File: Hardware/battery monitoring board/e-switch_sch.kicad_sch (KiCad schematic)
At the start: 5 parts, among them K1 Relay_SPST-NO, Q2 PN2222A

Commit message: added programmable LED and reference updates
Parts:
- renumbered D4 to D5, R14 to R15, R15 to R16
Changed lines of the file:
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@@
   (symbol (lib_id "power:GND") (at 86.36 88.9 0) (unit 1)
     (in_bom yes) (on_board yes) (dnp no) (fields_autoplaced)
-    (property "Reference" "#PWR023" (at 86.36 95.25 0)
+    (property "Reference" "#PWR024" (at 86.36 95.25 0)
       (effects (font (size 1.27 1.27)) hide)
     )
@@
       (project "battery monitoring board"
         (path "/bf623d80-ca5a-491f-9daa-4dffbeba5279/d1e89632-1041-42ed-815d-03472eda859a"
-          (reference "#PWR023") (unit 1)
+          (reference "#PWR024") (unit 1)
         )
       )
@@
   (symbol (lib_id "Device:R_US") (at 62.23 71.12 90) (unit 1)
     (in_bom yes) (on_board yes) (dnp no) (fields_autoplaced)
-    (property "Reference" "R14" (at 62.23 64.77 90)
+    (property "Reference" "R15" (at 62.23 64.77 90)
       (effects (font (size 1.27 1.27)))
     )
@@
       (project "battery monitoring board"
         (path "/bf623d80-ca5a-491f-9daa-4dffbeba5279/d1e89632-1041-42ed-815d-03472eda859a"
-          (reference "R14") (unit 1)
+          (reference "R15") (unit 1)
         )
       )
@@
   (symbol (lib_id "Device:D") (at 72.39 58.42 0) (unit 1)
     (in_bom yes) (on_board yes) (dnp no)
-    (property "Reference" "D4" (at 72.39 53.848 0)
+    (property "Reference" "D5" (at 72.39 53.848 0)
       (effects (font (size 1.27 1.27)))
     )
@@
       (project "battery monitoring board"
         (path "/bf623d80-ca5a-491f-9daa-4dffbeba5279/d1e89632-1041-42ed-815d-03472eda859a"
-          (reference "D4") (unit 1)
+          (reference "D5") (unit 1)
         )
       )
@@
   (symbol (lib_id "Device:R_US") (at 71.12 80.01 0) (unit 1)
     (in_bom yes) (on_board yes) (dnp no) (fields_autoplaced)
-    (property "Reference" "R15" (at 73.66 78.74 0)
+    (property "Reference" "R16" (at 73.66 78.74 0)
       (effects (font (size 1.27 1.27)) (justify left))
     )
@@
       (project "battery monitoring board"
         (path "/bf623d80-ca5a-491f-9daa-4dffbeba5279/d1e89632-1041-42ed-815d-03472eda859a"
-          (reference "R15") (unit 1)
+          (reference "R16") (unit 1)
         )
       )
@@
   (symbol (lib_id "PCM_4ms_Power-symbol:+9V") (at 49.53 45.72 90) (unit 1)
     (in_bom yes) (on_board yes) (dnp no) (fields_autoplaced)
-    (property "Reference" "#PWR022" (at 53.34 45.72 0)
+    (property "Reference" "#PWR023" (at 53.34 45.72 0)
       (effects (font (size 1.27 1.27)) hide)
     )
@@
       (project "battery monitoring board"
         (path "/bf623d80-ca5a-491f-9daa-4dffbeba5279/d1e89632-1041-42ed-815d-03472eda859a"
-          (reference "#PWR022") (unit 1)
+          (reference "#PWR023") (unit 1)
         )
       )

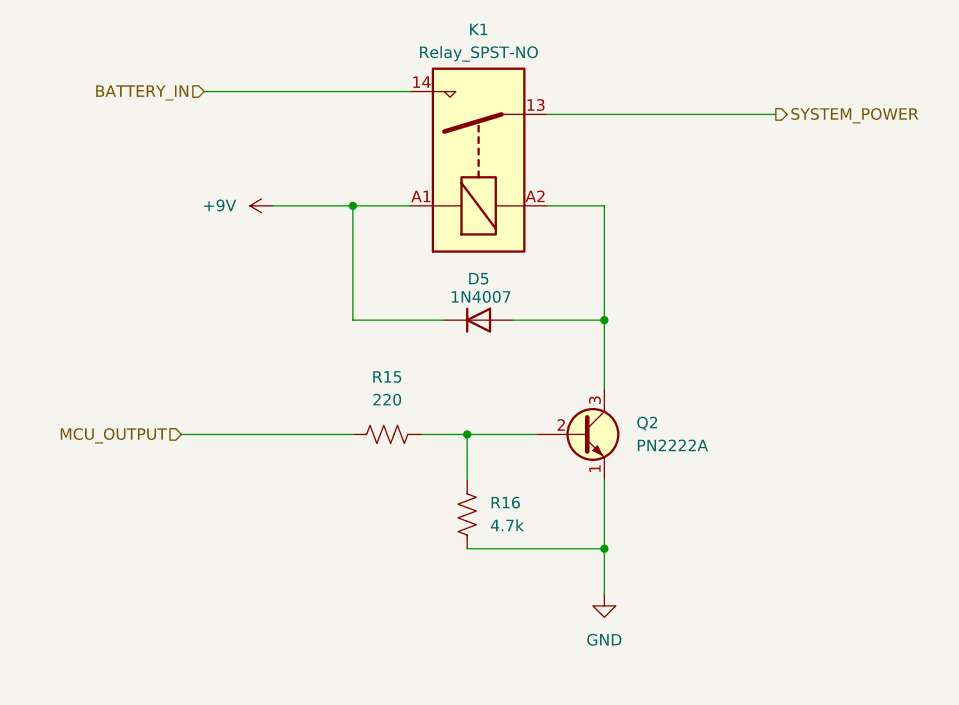
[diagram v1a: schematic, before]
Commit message: added test points (battery monitoring)
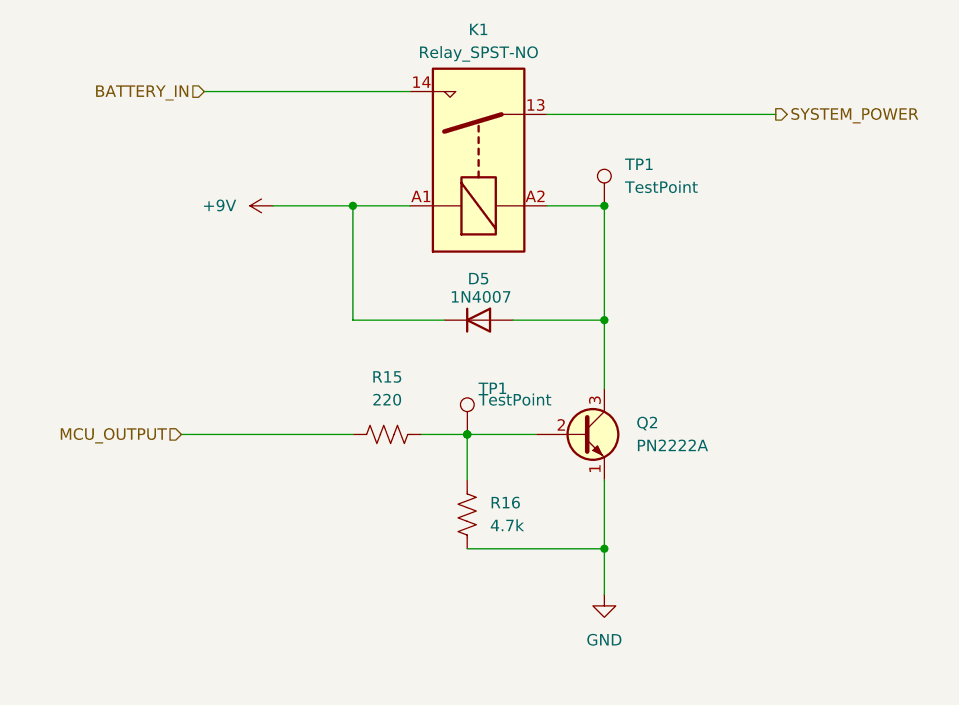
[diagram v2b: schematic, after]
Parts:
- added TP1 (x2): TestPoint, symbol Connector:TestPoint
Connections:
- net at Q2.2 (B), R15.2, R16.1: now also TP1.1
- net at D5.2 (A), K1.A2, Q2.3 (C): now also TP1.1
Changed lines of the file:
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@@
 (kicad_sch (version 20230121) (generator eeschema)
   (paper "A4")
+  (junction (at 86.36 45.72) (diameter 0) (color 0 0 0 0)
+  )
+  (junction (at 71.1341 71.12) (diameter 0) (color 0 0 0 0)
+  )
   (junction (at 86.36 58.42) (diameter 0) (color 0 0 0 0)
   )
@@
     (stroke (width 0) (type default))
   )
-  (wire (pts (xy 71.12 71.12) (xy 78.74 71.12))
+  (wire (pts (xy 71.12 71.12) (xy 71.1341 71.12))
     (stroke (width 0) (type default))
   )
@@
   )
   (wire (pts (xy 39.37 71.12) (xy 58.42 71.12))
+    (stroke (width 0) (type default))
+  )
+  (wire (pts (xy 71.1341 71.12) (xy 78.74 71.12))
     (stroke (width 0) (type default))
   )
@@
   (hierarchical_label "SYSTEM_POWER" (shape output) (at 105.41 35.56 0) (fields_autoplaced)
     (effects (font (size 1.27 1.27)) (justify left))
+  )
+  (symbol (lib_id "Connector:TestPoint") (at 86.36 45.72 0) (unit 1)
+    (in_bom yes) (on_board yes) (dnp no) (fields_autoplaced)
+    (property "Reference" "TP1" (at 88.6629 41.148 0)
+      (effects (font (size 1.27 1.27)) (justify left))
+    )
+    (property "Value" "TestPoint" (at 88.6629 43.688 0)
+      (effects (font (size 1.27 1.27)) (justify left))
+    )
+    (property "Footprint" "" (at 91.44 45.72 0)
+      (effects (font (size 1.27 1.27)) hide)
+    )
+    (property "Datasheet" "~" (at 91.44 45.72 0)
+      (effects (font (size 1.27 1.27)) hide)
+    )
+    (pin "1")
+    (instances
+      (project "battery monitoring board"
+        (path "/bf623d80-ca5a-491f-9daa-4dffbeba5279/5ec2dbdf-a276-4d4c-99fc-008475c1e770"
+          (reference "TP1") (unit 1)
+        )
+        (path "/bf623d80-ca5a-491f-9daa-4dffbeba5279/d1e89632-1041-42ed-815d-03472eda859a"
+          (reference "TP13") (unit 1)
+        )
+      )
+    )
   )
   (symbol (lib_id "power:GND") (at 86.36 88.9 0) (unit 1)
@@
         )
       )
+    )
+  )
+  (symbol (lib_id "Connector:TestPoint") (at 71.1341 71.12 0) (unit 1)
+    (in_bom yes) (on_board yes) (dnp no)
+    (property "Reference" "TP1" (at 72.39 66.04 0)
+      (effects (font (size 1.27 1.27)) (justify left))
+    )
+    (property "Value" "TestPoint" (at 72.39 67.31 0)
+      (effects (font (size 1.27 1.27)) (justify left))
+    )
+    (property "Footprint" "" (at 76.2141 71.12 0)
+      (effects (font (size 1.27 1.27)) hide)
+    )
+    (property "Datasheet" "~" (at 76.2141 71.12 0)
+      (effects (font (size 1.27 1.27)) hide)
+    )
+    (pin "1")
+    (instances
+      (project "battery monitoring board"
+        (path "/bf623d80-ca5a-491f-9daa-4dffbeba5279/5ec2dbdf-a276-4d4c-99fc-008475c1e770"
+          (reference "TP1") (unit 1)
+        )
+        (path "/bf623d80-ca5a-491f-9daa-4dffbeba5279/d1e89632-1041-42ed-815d-03472eda859a"
+          (reference "TP12") (unit 1)
+        )
+      )

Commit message: Added footprints to battery monitoring
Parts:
- D5: footprint (none) -> Diode_SMD:D_0805_2012Metric_Pad1.15x1.40mm_HandSolder
- K1: footprint (none) -> Library:Relay
- R15, R16: footprint (none) -> Resistor_SMD:R_0805_2012Metric_Pad1.20x1.40mm_HandSolder
- TP1: footprint (none) -> Library:Test Pads
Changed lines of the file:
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@@
       (effects (font (size 1.27 1.27)) (justify left))
     )
-    (property "Footprint" "" (at 91.44 45.72 0)
+    (property "Footprint" "Library:Test Pads" (at 91.44 45.72 0)
       (effects (font (size 1.27 1.27)) hide)
     )
@@
       (effects (font (size 1.27 1.27)) (justify left))
     )
-    (property "Footprint" "" (at 76.2141 71.12 0)
+    (property "Footprint" "Library:Test Pads" (at 76.2141 71.12 0)
       (effects (font (size 1.27 1.27)) hide)
     )
@@
       (effects (font (size 1.27 1.27)))
     )
-    (property "Footprint" "" (at 62.484 70.104 90)
+    (property "Footprint" "Resistor_SMD:R_0805_2012Metric_Pad1.20x1.40mm_HandSolder" (at 62.484 70.104 90)
       (effects (font (size 1.27 1.27)) hide)
     )
@@
       (effects (font (size 1.27 1.27)))
     )
-    (property "Footprint" "" (at 72.39 58.42 0)
+    (property "Footprint" "Diode_SMD:D_0805_2012Metric_Pad1.15x1.40mm_HandSolder" (at 72.39 58.42 0)
       (effects (font (size 1.27 1.27)) hide)
     )
@@
       (effects (font (size 1.27 1.27)))
     )
-    (property "Footprint" "" (at 73.66 29.21 0)
+    (property "Footprint" "Library:Relay" (at 73.66 29.21 0)
       (effects (font (size 1.27 1.27)) (justify left) hide)
     )
@@
       (effects (font (size 1.27 1.27)) (justify left))
     )
-    (property "Footprint" "" (at 72.136 80.264 90)
+    (property "Footprint" "Resistor_SMD:R_0805_2012Metric_Pad1.20x1.40mm_HandSolder" (at 72.136 80.264 90)
       (effects (font (size 1.27 1.27)) hide)
     )

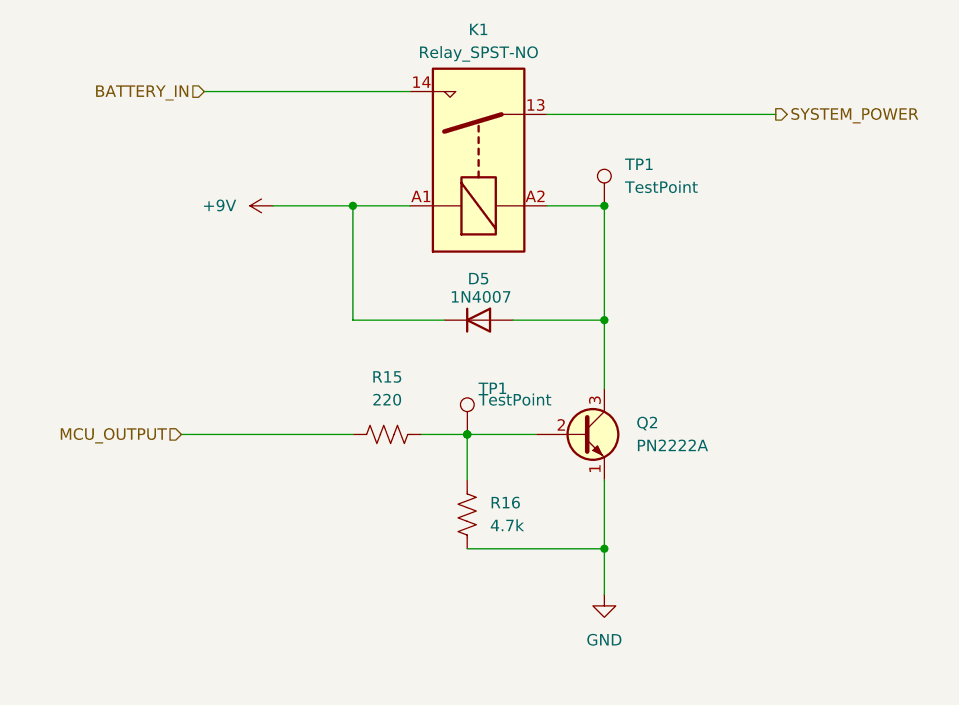
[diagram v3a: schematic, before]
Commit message: Added screw holes + other stuff
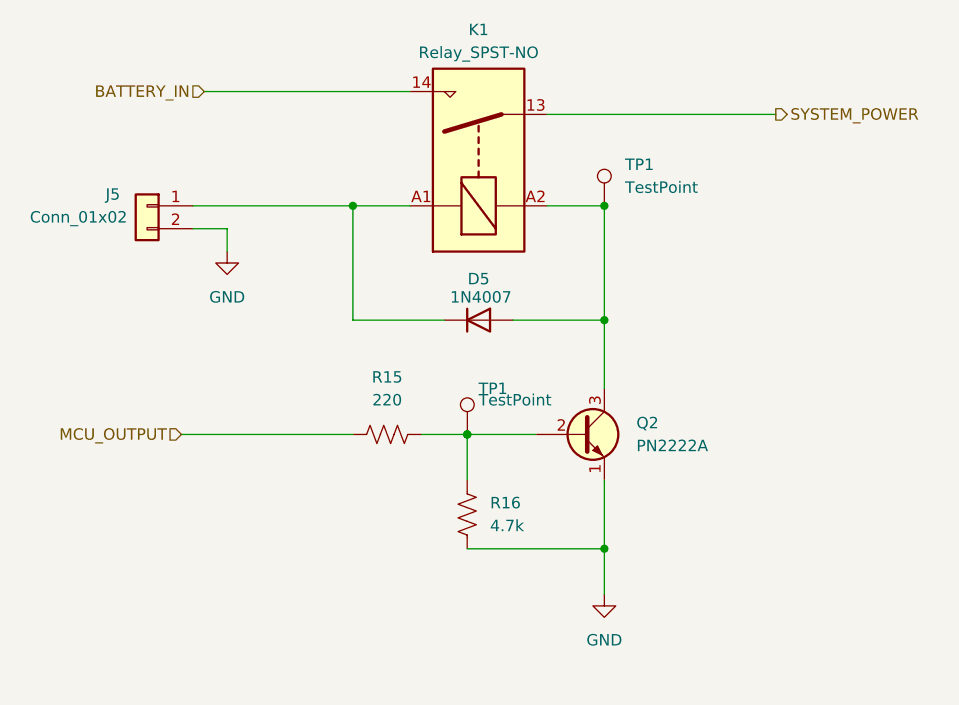
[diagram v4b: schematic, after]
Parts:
- added J5: Conn_01x02, Library:JST_BM02B-GHS-TBT_LF__SN_, symbol Connector_Generic:Conn_01x02
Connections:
- net GND: now also J5.2 (Pin_2)
- net +9V: no longer names the net of D5.1 (K), K1.A1
- net +9V: now also J5.1 (Pin_1)
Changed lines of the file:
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@@
     (stroke (width 0) (type default))
   )
-  (wire (pts (xy 49.53 45.72) (xy 58.42 45.72))
+  (wire (pts (xy 40.64 45.72) (xy 58.42 45.72))
     (stroke (width 0) (type default))
   )
@@
     (stroke (width 0) (type default))
   )
+  (wire (pts (xy 44.45 48.26) (xy 44.45 50.8))
+    (stroke (width 0) (type default))
+  )
   (wire (pts (xy 76.2 58.42) (xy 86.36 58.42))
     (stroke (width 0) (type default))
@@
   )
   (wire (pts (xy 58.42 45.72) (xy 64.77 45.72))
+    (stroke (width 0) (type default))
+  )
+  (wire (pts (xy 40.64 48.26) (xy 44.45 48.26))
     (stroke (width 0) (type default))
   )
@@
         (path "/bf623d80-ca5a-491f-9daa-4dffbeba5279/d1e89632-1041-42ed-815d-03472eda859a"
           (reference "Q2") (unit 1)
+        )
+      )
+    )
+  )
+  (symbol (lib_id "Connector_Generic:Conn_01x02") (at 35.56 45.72 0) (mirror y) (unit 1)
+    (in_bom yes) (on_board yes) (dnp no)
+    (property "Reference" "J5" (at 31.75 44.45 0)
+      (effects (font (size 1.27 1.27)))
+    )
+    (property "Value" "Conn_01x02" (at 27.94 46.99 0)
+      (effects (font (size 1.27 1.27)))
+    )
+    (property "Footprint" "Library:JST_BM02B-GHS-TBT_LF__SN_" (at 35.56 45.72 0)
+      (effects (font (size 1.27 1.27)) hide)
+    )
+    (property "Datasheet" "~" (at 35.56 45.72 0)
+      (effects (font (size 1.27 1.27)) hide)
+    )
+    (pin "1")
+    (pin "2")
+    (instances
+      (project "leak sensor"
+        (path "/127822e7-fd70-4fb4-952a-2fa8fdde2438"
+          (reference "J5") (unit 1)
+        )
+      )
+      (project "battery monitoring board"
+        (path "/bf623d80-ca5a-491f-9daa-4dffbeba5279/7fa71be0-4e2c-431c-85f4-b0f15423b53d"
+          (reference "J8") (unit 1)
+        )
+        (path "/bf623d80-ca5a-491f-9daa-4dffbeba5279/d1e89632-1041-42ed-815d-03472eda859a"
+          (reference "J10") (unit 1)
+        )
+      )
+    )
+  )
+  (symbol (lib_id "PCM_4ms_Power-symbol:GND") (at 44.45 50.8 0) (unit 1)
+    (in_bom yes) (on_board yes) (dnp no) (fields_autoplaced)
+    (property "Reference" "#PWR023" (at 44.45 57.15 0)
+      (effects (font (size 1.27 1.27)) hide)
+    )
+    (property "Value" "GND" (at 44.45 55.88 0)
+      (effects (font (size 1.27 1.27)))
+    )
+    (property "Footprint" "" (at 44.45 50.8 0)
+      (effects (font (size 1.27 1.27)) hide)
+    )
+    (property "Datasheet" "" (at 44.45 50.8 0)
+      (effects (font (size 1.27 1.27)) hide)
+    )
+    (pin "1")
+    (instances
+      (project "battery monitoring board"
+        (path "/bf623d80-ca5a-491f-9daa-4dffbeba5279/d1e89632-1041-42ed-815d-03472eda859a"
+          (reference "#PWR023") (unit 1)
         )
       )
@@
         )
       )
-    )
-  )
-  (symbol (lib_id "PCM_4ms_Power-symbol:+9V") (at 49.53 45.72 90) (unit 1)
-    (in_bom yes) (on_board yes) (dnp no) (fields_autoplaced)
-    (property "Reference" "#PWR023" (at 53.34 45.72 0)
-      (effects (font (size 1.27 1.27)) hide)
-    )
-    (property "Value" "+9V" (at 45.466 45.72 90)
-      (effects (font (size 1.27 1.27)) (justify left))
-    )
-    (property "Footprint" "" (at 49.53 45.72 0)
-      (effects (font (size 1.27 1.27)) hide)
-    )
-    (property "Datasheet" "" (at 49.53 45.72 0)
-      (effects (font (size 1.27 1.27)) hide)
-    )
-    (pin "1")
-    (instances
-      (project "battery monitoring board"
-        (path "/bf623d80-ca5a-491f-9daa-4dffbeba5279/d1e89632-1041-42ed-815d-03472eda859a"
-          (reference "#PWR023") (unit 1)
-        )
-      )

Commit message: silkscreen
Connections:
- net +9V: now reaches D5.1 (K), J5.1 (Pin_1), K1.A1
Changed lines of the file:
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@@
   (junction (at 86.36 83.82) (diameter 0) (color 0 0 0 0)
   )
+  (junction (at 44.45 45.72) (diameter 0) (color 0 0 0 0)
+  )
   (wire (pts (xy 86.36 76.2) (xy 86.36 83.82))
     (stroke (width 0) (type default))
@@
     (stroke (width 0) (type default))
   )
-  (wire (pts (xy 40.64 45.72) (xy 58.42 45.72))
+  (wire (pts (xy 40.64 45.72) (xy 44.45 45.72))
     (stroke (width 0) (type default))
   )
@@
     (stroke (width 0) (type default))
   )
+  (wire (pts (xy 44.45 45.72) (xy 58.42 45.72))
+    (stroke (width 0) (type default))
+  )
   (wire (pts (xy 86.36 83.82) (xy 86.36 88.9))
     (stroke (width 0) (type default))
@@
   )
   (wire (pts (xy 71.1341 71.12) (xy 78.74 71.12))
+    (stroke (width 0) (type default))
+  )
+  (wire (pts (xy 44.45 44.45) (xy 44.45 45.72))
     (stroke (width 0) (type default))
   )
@@
         )
       )
+    )
+  )
+  (symbol (lib_id "PCM_4ms_Power-symbol:+9V") (at 44.45 44.45 0) (unit 1)
+    (in_bom yes) (on_board yes) (dnp no) (fields_autoplaced)
+    (property "Reference" "#PWR030" (at 44.45 48.26 0)
+      (effects (font (size 1.27 1.27)) hide)
+    )
+    (property "Value" "+9V" (at 44.45 39.37 0)
+      (effects (font (size 1.27 1.27)))
+    )
+    (property "Footprint" "" (at 44.45 44.45 0)
+      (effects (font (size 1.27 1.27)) hide)
+    )
+    (property "Datasheet" "" (at 44.45 44.45 0)
+      (effects (font (size 1.27 1.27)) hide)
+    )
+    (pin "1")
+    (instances
+      (project "battery monitoring board"
+        (path "/bf623d80-ca5a-491f-9daa-4dffbeba5279/d1e89632-1041-42ed-815d-03472eda859a"
+          (reference "#PWR030") (unit 1)
+        )
+      )

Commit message: updated battery board pt.II
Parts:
- added D4: LED, Diode_SMD:D_0805_2012Metric_Pad1.15x1.40mm_HandSolder, symbol Device:LED
- added R10: 360, Resistor_SMD:R_0805_2012Metric_Pad1.20x1.40mm_HandSolder, symbol Device:R_US
- D7: renamed from D5; footprint Diode_SMD:D_0805_2012Metric_Pad1.15x1.40mm_HandSolder -> Diode_SMD:D_SMA
- J5: footprint Library:JST_BM02B-GHS-TBT_LF__SN_ -> Library:DEANS
- TP1: footprint Library:Test Pads -> PCM_4ms_TestPoint:TestPoint_Pad_06
- renumbered R15 to R17, R16 to R19
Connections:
- net +9V: now also R10.1
- net at D7.2 (A), K1.A2, Q2.3 (C)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: now also D4.1 (K)
- new net: D4.2 (A), R10.2
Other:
- moved on the sheet: D7, Q2, R17, R19, TP1

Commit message: erc-clear battery board
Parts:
- J5: value Conn_01x02 -> - 9V BAT +
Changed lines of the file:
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@@
       (effects (font (size 1.27 1.27)))
     )
-    (property "Value" "Conn_01x02" (at 27.94 46.99 0)
+    (property "Value" "- 9V BAT +" (at 27.94 46.99 0)
       (effects (font (size 1.27 1.27)))
     )
